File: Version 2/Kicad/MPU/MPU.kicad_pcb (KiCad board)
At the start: 2 copper layers, 19 parts, among them U2 MPU-6050, U3 AP2112K-3.3

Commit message: Modified: Routing
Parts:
- removed C3, C5: 10uF, Capacitor_SMD:CP_Elec_3x5.3
- removed C4: 2.2uF, Capacitor_SMD:CP_Elec_3x5.3
- removed C6, C7: 0.1uF, Capacitor_SMD:C_1812_4532Metric_Pad1.57x3.40mm_HandSolder
- removed R1: 1k, Resistor_THT:R_Axial_DIN0204_L3.6mm_D1.6mm_P1.90mm_Vertical
- removed R2, R3, R4: 4.7k, Resistor_THT:R_Axial_DIN0204_L3.6mm_D1.6mm_P1.90mm_Vertical
- removed R6: 4.7K, Resistor_THT:R_Axial_DIN0204_L3.6mm_D1.6mm_P1.90mm_Vertical
- removed the REF** at (103.9, 55.9)
- removed the REF** at (103.9, 91.2)
- removed U3: AP2112K-3.3, Package_TO_SOT_SMD:SOT-23-5
- added C10: 100nF, CL21A106KAYNNNE:CAPC2012X145N, F.Cu at (78.0, 70.0)
- added C11: 100nF, CL21A106KAYNNNE:CAPC2012X145N, F.Cu at (78.0, 57.5)
- added C8: 2.2uF, CL21A106KAYNNNE:CAPC2012X145N, F.Cu at (78.0, 61.0)
- added C9: 100nF, CL21A106KAYNNNE:CAPC2012X145N, F.Cu at (84.2, 67.0)
- added R7: 4.7k, 8-1879533-1:RESC1608X50N, F.Cu at (78.2, 65.0)
- added R8: 4.7k, 8-1879533-1:RESC1608X50N, F.Cu at (90.5, 67.0)
- added R9: 1k, 8-1879533-1:RESC1608X50N, F.Cu at (84.3, 70.0)
- added REF**: MountingHole_2.1mm, MountingHole:MountingHole_2.1mm, F.Cu at (94.2, 72.0)
- added REF**: MountingHole_2.1mm, MountingHole:MountingHole_2.1mm, F.Cu at (94.0, 49.9)
- added U1: AMS1117-3.3, Package_TO_SOT_SMD:SOT-223-3_TabPin2, F.Cu at (86.5, 53.5)
- C1: footprint Capacitor_SMD:CP_Elec_4x5.4 -> CL21A106KAYNNNE:CAPC2012X145N
- C2: value 0.1uF -> 10uF; footprint Capacitor_SMD:C_1812_4532Metric_Pad1.57x3.40mm_HandSolder -> CL21A106KAYNNNE:CAPC2012X145N
- D2: footprint LED_THT:LED_D1.8mm_W1.8mm_H2.4mm_Horizontal_O1.27mm_Z8.2mm -> CL21A106KAYNNNE:CAPC2012X145N
- R5: footprint Resistor_THT:R_Axial_DIN0204_L3.6mm_D1.6mm_P1.90mm_Vertical -> 8-1879533-1:RESC1608X50N
- moved D2 15.7 mm to (89.2, 69.8)
- moved C1 12.6 mm to (78.0, 52.0), turned to 180 degrees
- moved C2 11.7 mm to (91.2, 60.0)
- moved PINS 10.5 mm to (74.0, 52.5)
- moved U2 7.41 mm to (85.2, 61.0)
- moved R5 4.40 mm to (90.7, 64.0)
- renumbered PIN1 to PINS
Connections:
- C1 pad 1: VCC -> GND
- C1 pad 2: Earth -> VCC
- C2 pad 1: +3.3V -> GND
- C2 pad 2: Earth -> +3.3V
- D2 pad 1: Earth -> GND
- PINS pad 8: unconnected-(PIN1-Pin_8-Pad8) -> /INT
- R5 pad 1: Net-(U2-AUX_DA) -> +3.3V
- R5 pad 2: +3.3V -> /SDA
- U2 pad 1: Earth -> GND
- U2 pad 11: Earth -> GND
- U2 pad 12: unconnected-(U2-INT-Pad12) -> /INT
- U2 pad 9: unconnected-(U2-AD0-Pad9) -> /AD0
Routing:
- net GND: track 0.00 -> 112.6 mm, vias 0 -> 3
- net +3.3V: track 0.00 -> 81.2 mm, vias 0 -> 3
- net /SDA: track 0.00 -> 28.9 mm, vias 0 -> 3
- net /SCL: track 0.00 -> 22.4 mm, vias 0 -> 2
- net Net-(PIN1-Pin_7): track 0.00 -> 21.7 mm, vias 0 -> 2
- net /INT: track 0.00 -> 18.0 mm
- net Net-(U2-CPOUT): track 0.00 -> 17.4 mm, vias 0 -> 1
- net VCC: track 0.00 -> 16.3 mm
- net (no net): track 0.00 -> 16.2 mm
- net /XCL: track 0.00 -> 11.7 mm
- net /XDA: track 0.00 -> 9.93 mm, vias 0 -> 1
- net Net-(D2-A): track 0.00 -> 5.46 mm
- net Net-(U2-REGOUT): track 0.00 -> 5.26 mm, vias 0 -> 1
- added copper zone on F.Cu, net +3.3V
- added copper zone on F.Cu, net GND
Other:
- board outline added: 61 x 33.2 mm

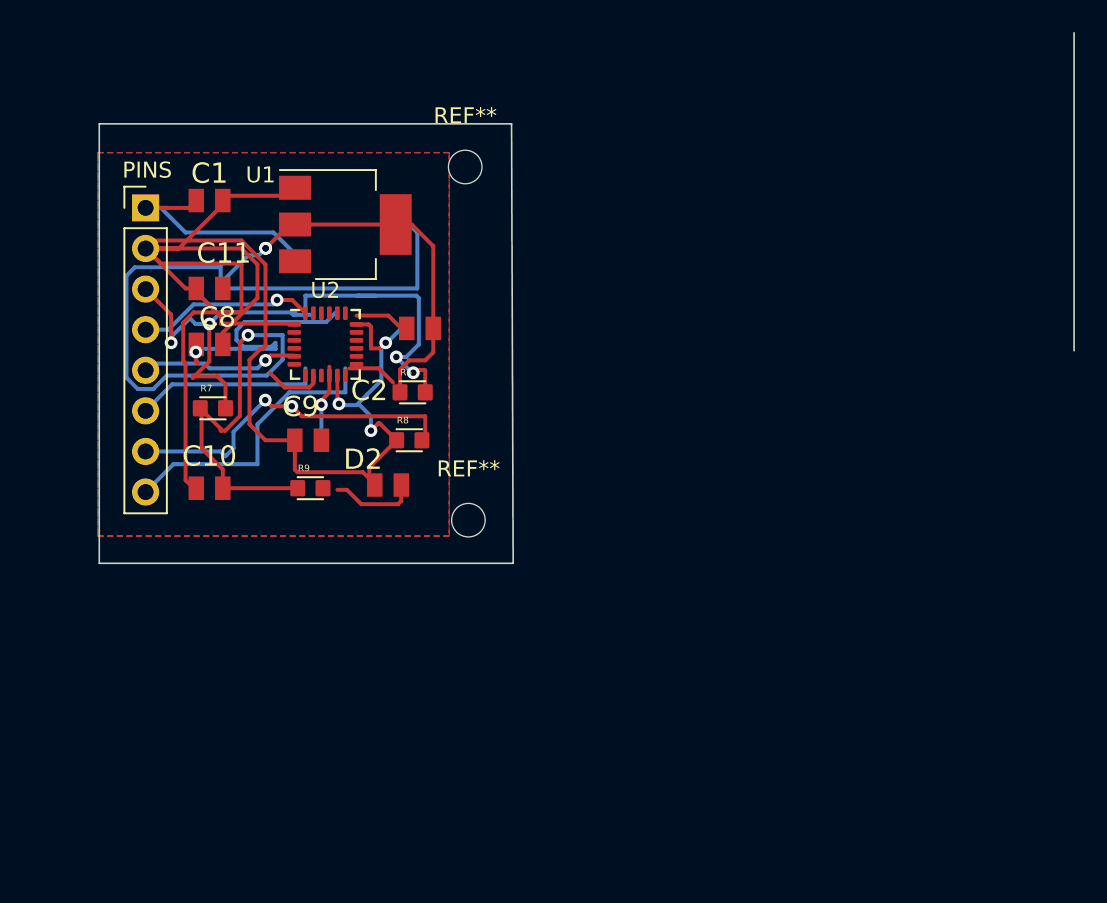
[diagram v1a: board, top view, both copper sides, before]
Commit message: Modified: Correcting design rules errors
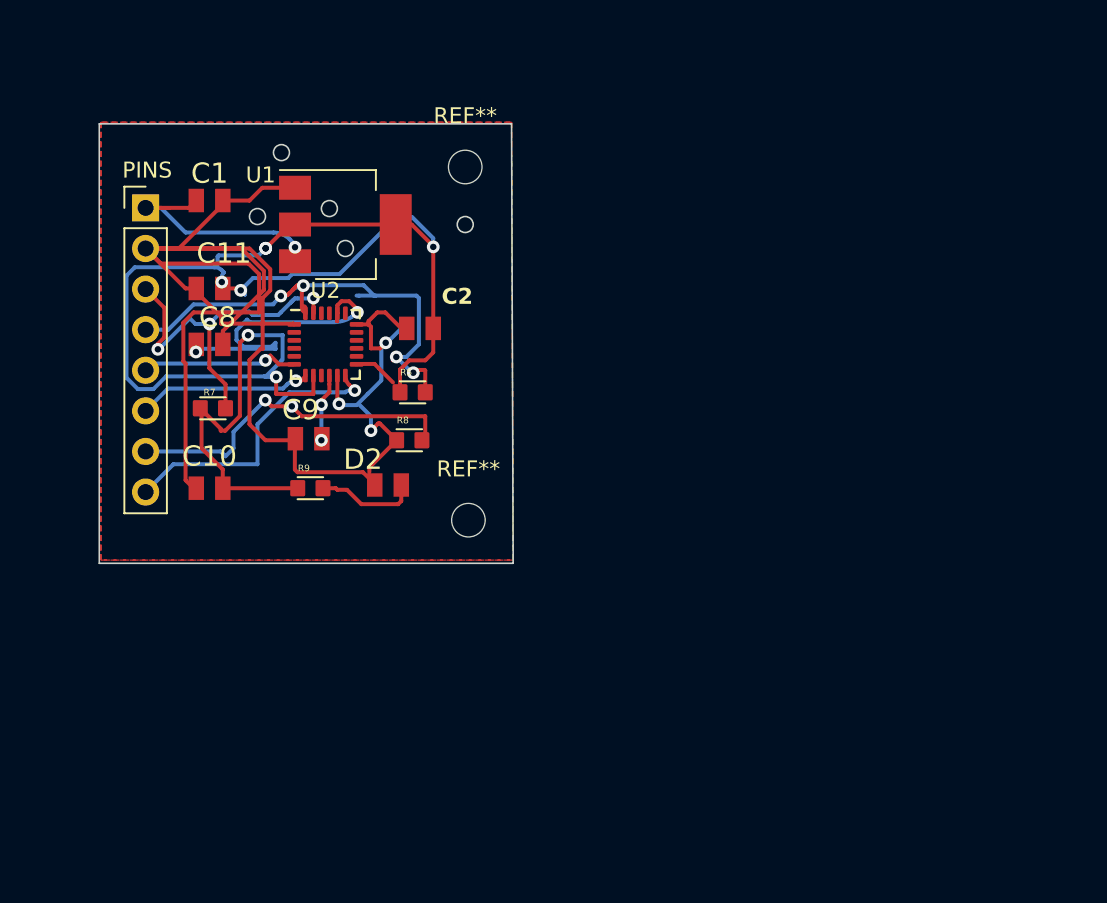
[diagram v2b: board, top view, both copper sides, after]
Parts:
- moved C9 0.10 mm to (84.2, 66.9)
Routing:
- net +3.3V: track 81.2 -> 99.6 mm, vias 3 -> 7
- net (no net): track 16.2 -> 0.00 mm
- net /SDA: track 28.9 -> 31.9 mm, vias 3 -> 4
- net Net-(U2-CPOUT): track 17.4 -> 19.9 mm, vias 1 -> 2
- net GND: track 112.6 -> 114.6 mm
- net Net-(D2-A): track 5.46 -> 6.40 mm
- net /SCL: track 22.4 -> 23.2 mm, vias 2 -> 3
- net /XCL: track 11.7 -> 11.0 mm, vias 0 -> 1
- net Net-(U2-REGOUT): track 5.26 -> 4.71 mm, vias 1 -> 2
- net /INT: track 18.0 -> 18.3 mm, vias 0 -> 1
- net VCC: track 16.3 -> 16.2 mm, vias 0 -> 1
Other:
- board size 61 x 33.2 mm -> 25.9 x 27.5 mm

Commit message: Modified: no warning or errors detected
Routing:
- net VCC: track 16.2 -> 20.8 mm, vias 1 -> 2
- net GND: track 114.6 -> 110.1 mm
- net /SDA: track 31.9 -> 28.2 mm, vias 4 -> 3
- net +3.3V: track 99.6 -> 100.7 mm, vias 7 -> 6
- net Net-(PIN1-Pin_7): vias 2 -> 1

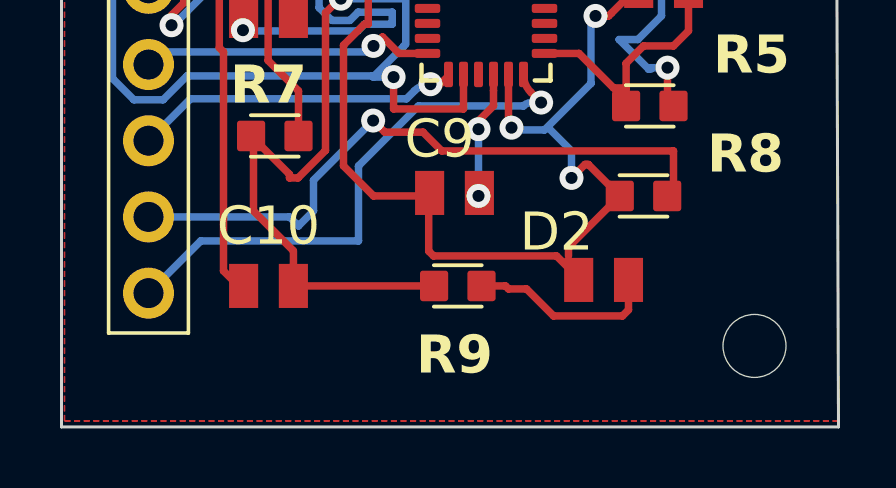
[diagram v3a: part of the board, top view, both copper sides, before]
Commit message: Modified: adding title
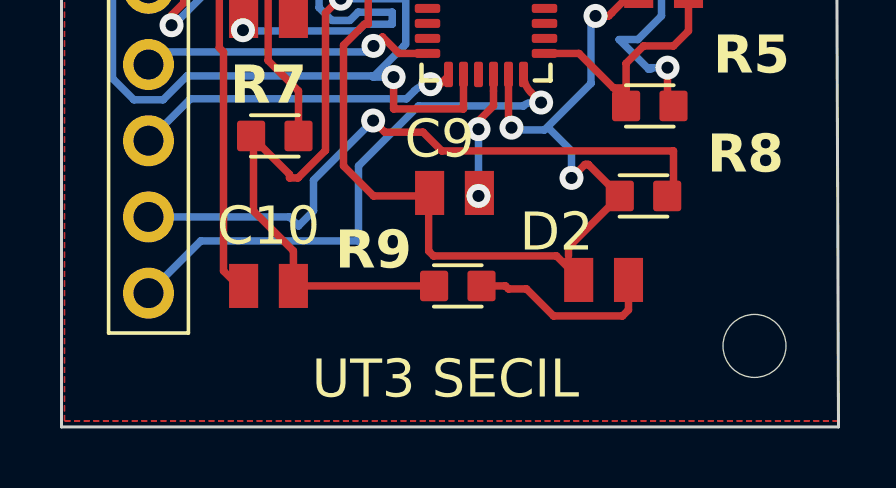
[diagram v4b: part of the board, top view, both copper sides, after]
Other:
- board text added: "UT3 SECIL"
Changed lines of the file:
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@@
     (property "Sheetname" "")
     (attr smd)
-    (fp_text reference "R9" (at -0.11 2.3) (layer "F.SilkS")
+    (fp_text reference "R9" (at -2.81 -1.2) (layer "F.SilkS")
         (effects (font (size 1.27 1.27) (thickness 0.254) bold))
     )
@@
   (gr_line (start 71.1 47.2) (end 96.9 47.2)
     (stroke (width 0.1) (type default)) (layer "Edge.Cuts"))
+  (gr_text "UT3 SECIL\n" (at 83.9 73.1) (layer "F.SilkS")
+    (effects (font (size 1.27 1.27) (thickness 0.254)))
+  )
   (segment (start 83.42 70) (end 78.83 70) (width 0.25) (layer "F.Cu") (net 5))
   (segment (start 78.984555 66.4) (end 79.9 65.484555) (width 0.25) (layer "F.Cu") (net 5))

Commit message: Modified: rerouting the pcb
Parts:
- removed the REF** at (94.2, 72.0)
- removed the REF** at (94.0, 49.9)
- added REF**: MountingHole_3.2mm_M3, MountingHole:MountingHole_3.2mm_M3, F.Cu at (94.6, 49.4)
- added REF**: MountingHole_3.2mm_M3, MountingHole:MountingHole_3.2mm_M3, F.Cu at (94.6, 72.4)
- moved R8 13.0 mm to (77.6, 65.4), turned to -90 degrees
- moved R5 12.5 mm to (81.4, 55.6), turned to -90 degrees
- moved D2 11.6 mm to (77.6, 69.0), turned to -90 degrees
- moved C11 11.5 mm to (88.2, 62.8)
- moved R7 8.61 mm to (78.6, 56.4), turned to 180 degrees
- moved C2 7.79 mm to (88.2, 67.2)
- moved C8 6.43 mm to (84.4, 61.6), turned to -90 degrees
- moved U2 5.66 mm to (79.6, 60.6)
- moved C10 5.22 mm to (80.8, 65.6)
- moved R9 2.63 mm to (81.8, 69.2), turned to -90 degrees
- moved U1 2.20 mm to (87.6, 55.4), turned to 180 degrees
- moved C1 1.52 mm to (78.6, 53.4), turned to 90 degrees
- moved C9 0.51 mm to (84.4, 66.4), turned to 90 degrees
- moved PIN1 0.10 mm to (74.0, 52.6)
- renumbered PINS to PIN1
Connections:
- PIN1 pad 1: VCC -> GND
- PIN1 pad 2: GND -> VCC
- PIN1 pad 7: Net-(PIN1-Pin_7) -> /AD0
- R8 pad 2: Net-(PIN1-Pin_7) -> /AD0
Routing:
- net GND: track 110.1 -> 38.9 mm, vias 3 -> 10
- net +3.3V: track 100.7 -> 53.6 mm, vias 6 -> 2
- net Net-(PIN1-Pin_7): track 21.7 -> 0.00 mm, vias 1 -> 0
- net /SDA: track 28.2 -> 11.0 mm, vias 3 -> 2
- net /SCL: track 22.8 -> 6.95 mm, vias 3 -> 0
- net Net-(U2-CPOUT): track 20.0 -> 6.52 mm, vias 2 -> 0
- net /AD0: track 0.00 -> 13.1 mm, vias 0 -> 1
- net /INT: track 18.3 -> 25.6 mm, vias 1 -> 0
- net /XDA: track 9.91 -> 3.97 mm, vias 1 -> 0
- net /XCL: track 11.0 -> 5.47 mm, vias 1 -> 0
- net Net-(D2-A): track 6.40 -> 4.25 mm
- net Net-(U2-REGOUT): track 4.71 -> 6.21 mm, vias 2 -> 0
- net VCC: track 20.8 -> 20.1 mm, vias 2 -> 0
- added copper zone on B.Cu, net GND
- removed copper zone on F.Cu, net +3.3V
- removed copper zone on F.Cu, net GND
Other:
- outline, holes or cut-outs redrawn
